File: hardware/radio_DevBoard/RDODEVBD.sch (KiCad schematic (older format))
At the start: 21 parts, among them J1 SMA, P1 CONN_01X08, U1 AX5043, X1 CRYSTAL_SMD

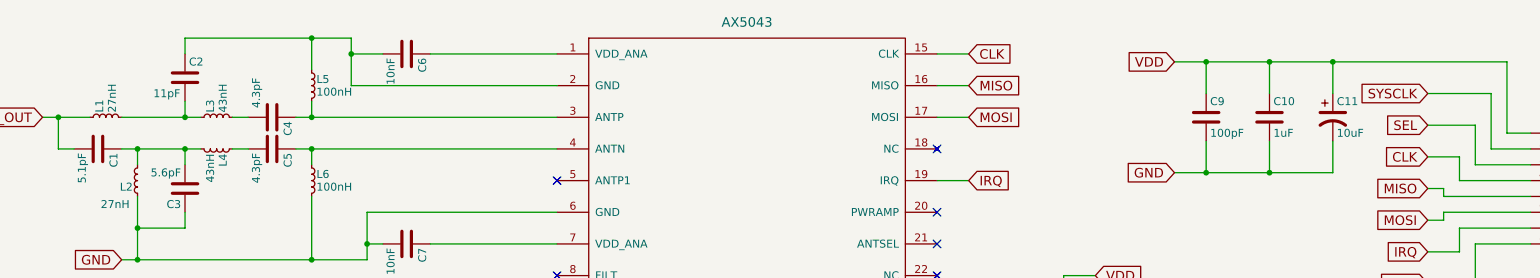
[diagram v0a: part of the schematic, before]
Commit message: Finished Radio Interface Dev & Audio Dev Schematic
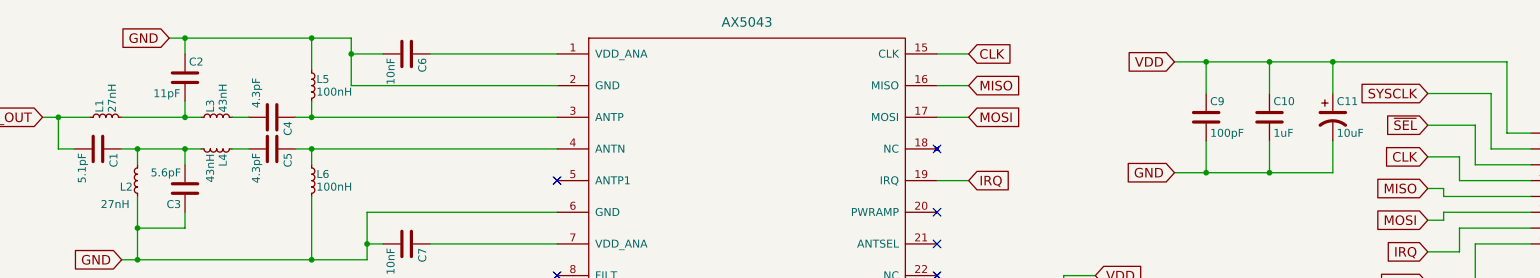
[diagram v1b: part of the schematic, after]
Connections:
- net SEL is gone; now on net ~SEL: P1.3 (P3)
- net GND: now also C2.1, C6.2, L5.1, U1.2 (GND)
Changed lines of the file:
@@
 	2250 1550 2250 1450
 Wire Wire Line
-	2250 1450 3300 1450
+	2150 1450 3300 1450
 Wire Wire Line
 	3050 1650 3050 1450
@@
 SYSCLK
 Text GLabel 10100 2000 0    60   Input ~ 0
-SEL
+~SEL
 Text GLabel 10100 2200 0    60   Input ~ 0
 CLK
@@
 Text GLabel 8500 2300 0    60   Input ~ 0
 GND
+Connection ~ 2250 1450
+Text GLabel 2150 1450 0    60   Input ~ 0
+GND
 $EndSCHEMATC

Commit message: Added Battery Charger
Added MCP73833 to Schematic
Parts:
- added C12, C13: 10uF, symbol C
- added CN1: USB_B, symbol USB_B
- added CN2: BATT_IN_JST, symbol PWR_IN_0.1
- added CN3: LOAD_JST, symbol PWR_IN_0.1
- added JP11: PWR_IN_0.1, symbol PWR_IN_0.1
- added JP3: LOAD_0.1, symbol PWR_IN_0.1
- added JP5: BATT_IN_0.1, symbol PWR_IN_0.1
- added JP6: STAT, symbol PWR_IN_0.1
- added R1, R2, R3, RT1: 1K, symbol R
- added R4: 2K, symbol R
- added R7: 10K/THERM, symbol R
- added RT2: 150K, symbol R
- added STAT1-ORANGE1: LED1, symbol LED
- added STAT2-GREEN1: LED2, symbol LED
- added STAT2-RED1: LED3, symbol LED
- added U1: MCP73833T-AMI/MF, symbol MCP73833T-AMI/MF-RESCUE-RDODEVBD
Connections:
- net labels added: +5V
- wire segments 88 -> 148
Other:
- note added: "10K = 100mA\n5.0K = 200mA\n2.0K = 500mA\n1.0K = 1000mA"
- note added: "No Thermistor\nRT1 = 0 RT2 = NC THERM = 10K\n10K NTC THERMISTOR\nRT1 = TBD RT2 = TBD"

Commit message: Added Audio Card
Added MP45T02 to schematic
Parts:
- added C14: 100nF, symbol C
- added C15: 10uF, symbol C
- added R5, R6: 0, symbol R
- added U91: MP45DT02, symbol MP45DT02
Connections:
- net labels added: +3.3V, PB10, PC3
- wire segments 148 -> 166
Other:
- note added: "Not Fitted"
- note added: "PDM_OUT\nCLK_IN"
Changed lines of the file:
@@
 LIBS:MCP73833T
 LIBS:PWR_IN_0.1
+LIBS:mp45dt02
 LIBS:RDODEVBD-cache
 EELAYER 25 0
@@
 Wire Wire Line
 	1200 7000 1250 7000
+$Comp
+L MP45DT02 U91
+U 1 1 58A3B9C5
+P 9200 5550
+F 0 "U91" H 9000 5700 60  0000 C CNN
+F 1 "MP45DT02" H 9250 5300 60  0000 C CNN
+F 2 "" H 9200 5550 60  0001 C CNN
+F 3 "" H 9200 5550 60  0001 C CNN
+	1    9200 5550
+	1    0    0    -1
+$EndComp
+$Comp
+L R R5
+U 1 1 58A3F4FF
+P 8300 5450
+F 0 "R5" V 8380 5450 50  0000 C CNN
+F 1 "0" V 8200 5450 50  0000 C CNN
+F 2 "" V 8230 5450 50  0000 C CNN
+F 3 "" H 8300 5450 50  0000 C CNN
+	1    8300 5450
+	1    0    0    -1
+$EndComp
+$Comp
+L R R6
+U 1 1 58A3FA53
+P 8300 5850
+F 0 "R6" V 8380 5850 50  0000 C CNN
+F 1 "0" V 8200 5850 50  0000 C CNN
+F 2 "" V 8230 5850 50  0000 C CNN
+F 3 "" H 8300 5850 50  0000 C CNN
+	1    8300 5850
+	1    0    0    -1
+$EndComp
+Wire Wire Line
+	8300 5600 8300 5700
+Wire Wire Line
+	8300 6000 8300 6050
+Wire Wire Line
+	8300 6050 8900 6050
+Wire Wire Line
+	8700 6050 8700 5000
+Connection ~ 8700 5700
+Wire Wire Line
+	8700 5600 8400 5600
+Wire Wire Line
+	8400 5600 8400 5650
+Wire Wire Line
+	8400 5650 8300 5650
+Connection ~ 8300 5650
+Connection ~ 8700 5600
+$Comp
+L C C15
+U 1 1 58A40B4F
+P 9250 5250
+F 0 "C15" H 9275 5350 50  0000 L CNN
+F 1 "10uF" H 9275 5150 50  0000 L CNN
+F 2 "" H 9288 5100 50  0000 C CNN
+F 3 "" H 9250 5250 50  0000 C CNN
+	1    9250 5250
+	0    1    1    0
+$EndComp
+$Comp
+L C C14
+U 1 1 58A41D99
+P 9250 5000
+F 0 "C14" H 9275 5100 50  0000 L CNN
+F 1 "100nF" H 9275 4900 50  0000 L CNN
+F 2 "" H 9288 4850 50  0000 C CNN
+F 3 "" H 9250 5000 50  0000 C CNN
+	1    9250 5000
+	0    1    1    0
+$EndComp
+Text GLabel 9950 5600 2    60   Input ~ 0
+PC3
+Text GLabel 9950 5800 2    60   Input ~ 0
+PB10
+Wire Wire Line
+	9650 5600 9950 5600
+Wire Wire Line
+	9650 5700 9800 5700
+Wire Wire Line
+	9800 5700 9800 5800
+Wire Wire Line
+	9800 5800 9950 5800
+Wire Wire Line
+	8700 5000 9100 5000
+Connection ~ 8700 5500
+Wire Wire Line
+	9100 5250 8700 5250
+Connection ~ 8700 5250
+Wire Wire Line
+	9400 5250 9700 5250
+Wire Wire Line
+	9700 4900 9700 5500
+Wire Wire Line
+	9700 5500 9650 5500
+Wire Wire Line
+	9700 5000 9400 5000
+Connection ~ 9700 5250
+Text GLabel 8900 6050 2    60   Input ~ 0
+GND
+Connection ~ 8700 6050
+Text Notes 10300 5750 0    60   ~ 0
+PDM_OUT\nCLK_IN
+Text Notes 7750 5400 0    60   ~ 0
+Not Fitted
+$Comp
+L +3.3V #PWR?
+U 1 1 58A43526
+P 8300 5200
+F 0 "#PWR?" H 8300 5050 50  0001 C CNN
+F 1 "+3.3V" H 8300 5340 50  0000 C CNN
+F 2 "" H 8300 5200 50  0000 C CNN
+F 3 "" H 8300 5200 50  0000 C CNN
+	1    8300 5200
+	1    0    0    -1
+$EndComp
+$Comp
+L +3.3V #PWR?
+U 1 1 58A435C2
+P 9700 4900
+F 0 "#PWR?" H 9700 4750 50  0001 C CNN
+F 1 "+3.3V" H 9700 5040 50  0000 C CNN
+F 2 "" H 9700 4900 50  0000 C CNN
+F 3 "" H 9700 4900 50  0000 C CNN
+	1    9700 4900
+	1    0    0    -1
+$EndComp
+Connection ~ 9700 5000
+Wire Wire Line
+	8300 5200 8300 5300
 $EndSCHEMATC
